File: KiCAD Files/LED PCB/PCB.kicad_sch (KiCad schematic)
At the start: 51 parts, among them J1 Conn_01x18_Male, J2 Conn_01x18_Male, SW1 SW_Push, SW2 SW_Push, SW3 SW_Push, SW4 SW_Push, SW5 SW_Push, SW6 SW_Push, SW7 SW_Push

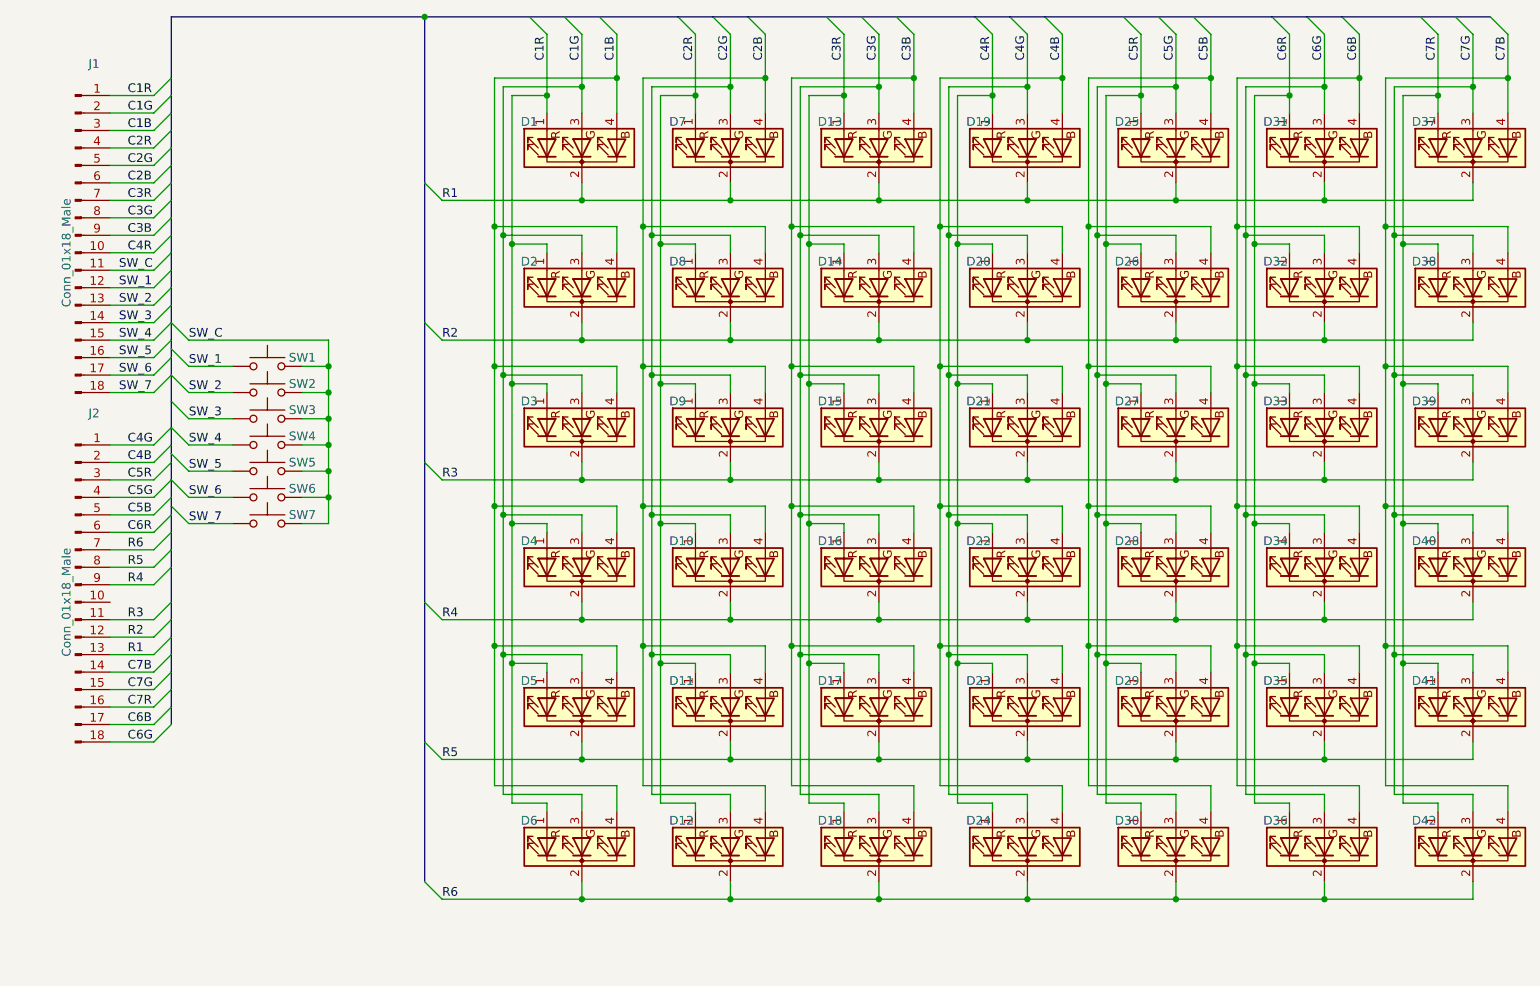
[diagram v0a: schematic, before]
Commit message: Updated schematic. Added tooloing hole for driver for potential assembly. Added rev number
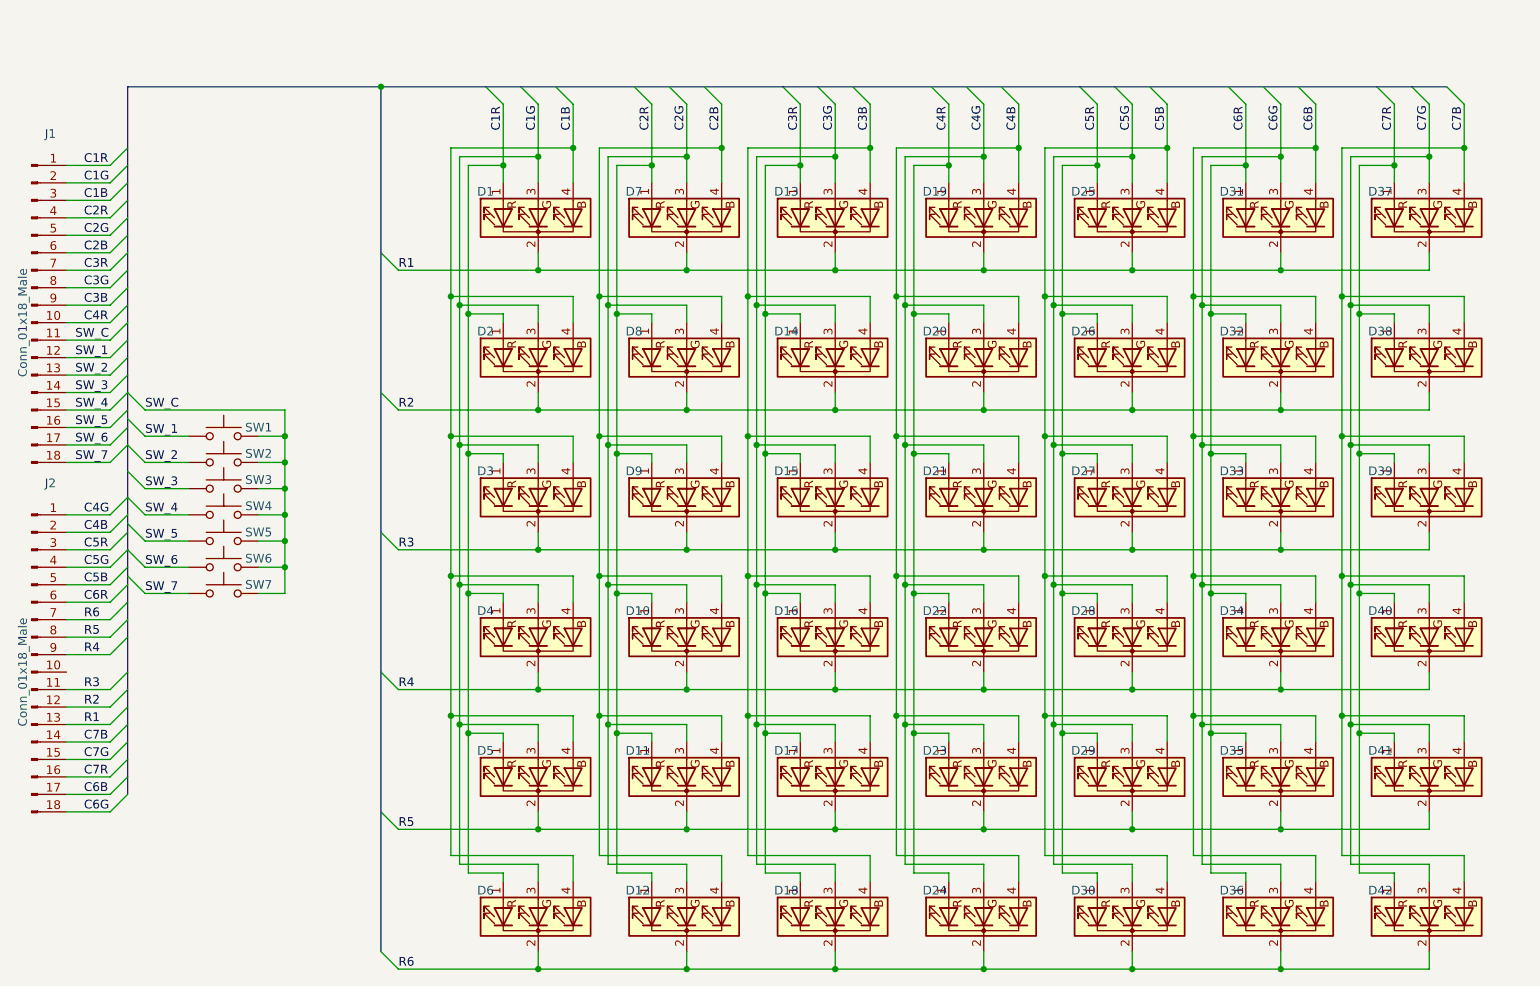
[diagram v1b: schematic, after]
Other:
- company: (none) -> Designed by Electro707 (Jamal Bouajjaj)
- title: (none) -> 4-In-A-Row Soldering Kit LED Board
- moved on the sheet: D1, D10, D11, D12, D13, D14, D15, D16, D17, D18, D19, D2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

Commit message: Updated KiCAD files for KiCAD 6
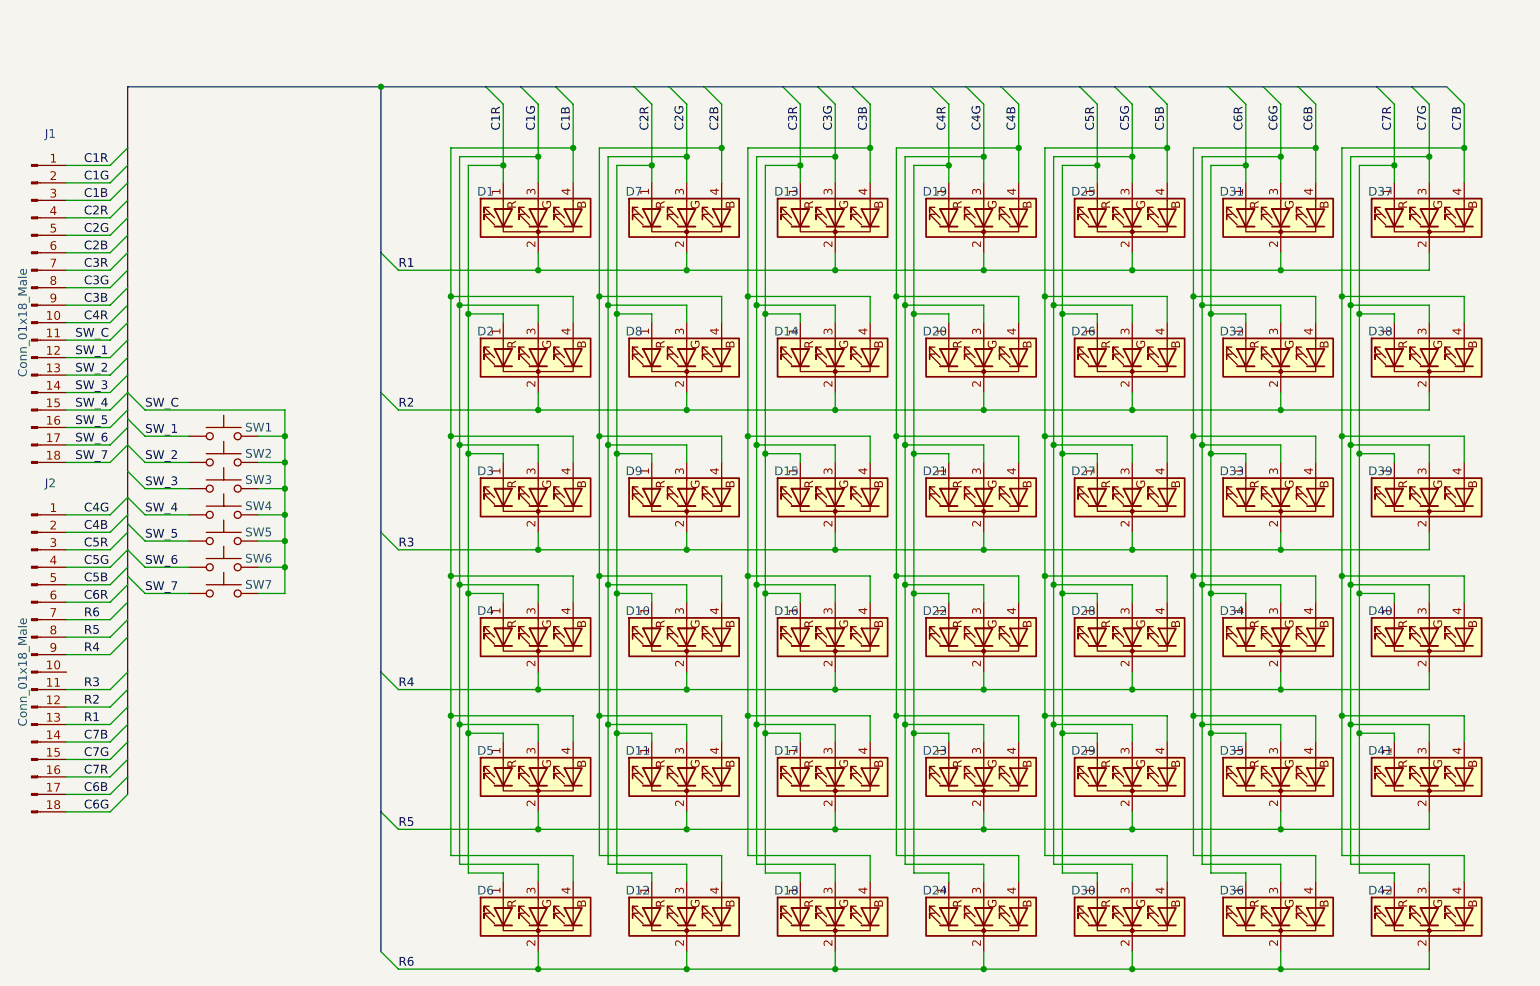
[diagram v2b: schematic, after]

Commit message: Updated titleblock. Fixed R9 value on driver. Added polyfuse's part number
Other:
- company: Designed by Electro707 (Jamal Bouajjaj) -> (none)
